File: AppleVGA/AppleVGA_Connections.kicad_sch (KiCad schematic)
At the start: 7 parts, among them J1 AppleIIBus, J2 VGA, J3 VGA, SW1 SW_Push

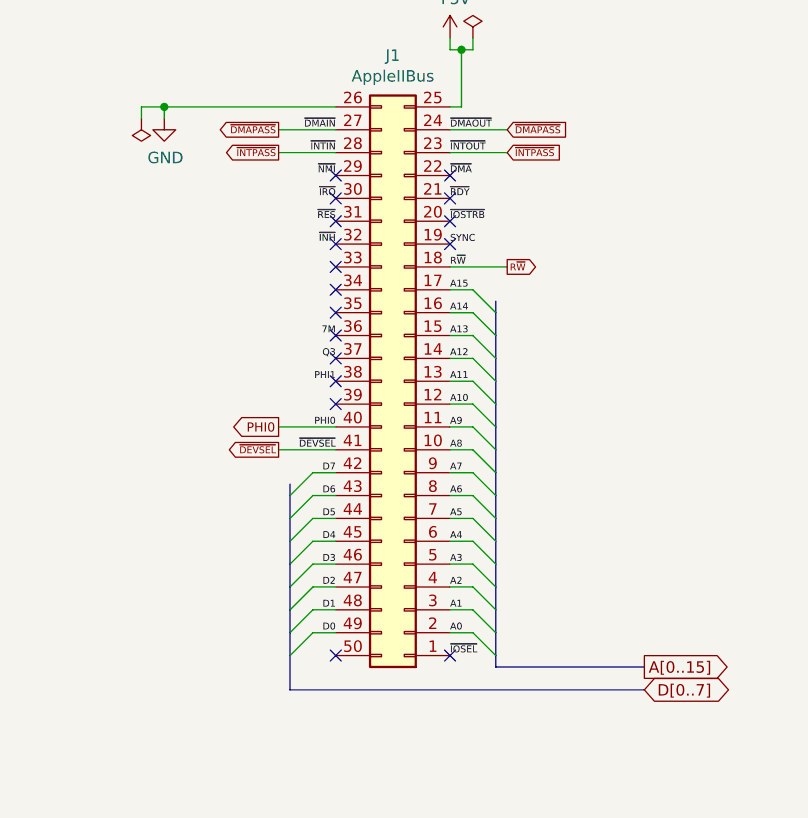
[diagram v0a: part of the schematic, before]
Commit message: Minor cleanups after KiCad6 conversion
* Fixed the 3.3v net symbol that changed in KiCad6
* Updated the Pico symbol & footprint to the latest version
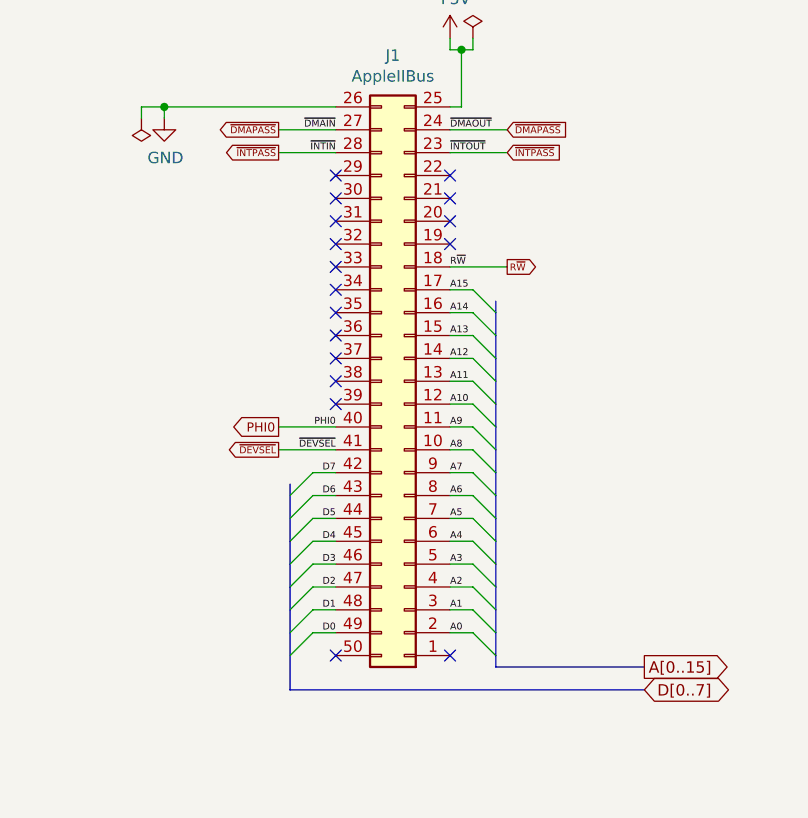
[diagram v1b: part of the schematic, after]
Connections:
- net +3V3 renamed +3.3V
- net 7M: no longer names the net of J1.36 (Pin_36)
- net PHI1: no longer names the net of J1.38 (Pin_38)
- net Q3: no longer names the net of J1.37 (Pin_37)
- net SYNC: no longer names the net of J1.19 (Pin_19)
- net ~{DMA}: no longer names the net of J1.22 (Pin_22)
- net ~{INH}: no longer names the net of J1.32 (Pin_32)
- net ~{IOSEL}: no longer names the net of J1.1 (Pin_1)
- net ~{IOSTRB}: no longer names the net of J1.20 (Pin_20)
- net ~{IRQ}: no longer names the net of J1.30 (Pin_30)
- net ~{NMI}: no longer names the net of J1.29 (Pin_29)
- net ~{RDY}: no longer names the net of J1.21 (Pin_21)
- net ~{RES}: no longer names the net of J1.31 (Pin_31)
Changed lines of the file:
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@@
   )
   (no_connect (at 60.96 77.47))
+  (no_connect (at 60.96 95.25))
+  (no_connect (at 60.96 90.17))
+  (no_connect (at 60.96 87.63))
+  (no_connect (at 73.66 77.47))
+  (no_connect (at 73.66 80.01))
+  (no_connect (at 73.66 74.93))
+  (no_connect (at 73.66 72.39))
   (no_connect (at 60.96 74.93))
-  (no_connect (at 60.96 87.63))
-  (no_connect (at 73.66 80.01))
+  (no_connect (at 60.96 72.39))
   (no_connect (at 60.96 125.73))
-  (no_connect (at 60.96 95.25))
-  (no_connect (at 73.66 77.47))
   (no_connect (at 207.01 86.36))
   (no_connect (at 191.77 93.98))
-  (no_connect (at 60.96 90.17))
-  (no_connect (at 73.66 125.73))
-  (no_connect (at 73.66 72.39))
+  (no_connect (at 60.96 80.01))
   (no_connect (at 60.96 82.55))
   (no_connect (at 207.01 81.28))
   (no_connect (at 60.96 97.79))
   (no_connect (at 191.77 96.52))
+  (no_connect (at 207.01 101.6))
   (no_connect (at 60.96 92.71))
-  (no_connect (at 207.01 101.6))
-  (no_connect (at 60.96 72.39))
-  (no_connect (at 60.96 80.01))
   (no_connect (at 60.96 85.09))
-  (no_connect (at 73.66 74.93))
+  (no_connect (at 73.66 125.73))
   (bus_entry (at 76.2 113.03) (size 2.54 2.54)
     (stroke (width 0) (type default) (color 0 0 0 0))
@@
     (effects (font (size 0.762 0.762)) (justify right bottom))
   )
-  (label "~{RES}" (at 60.96 77.47 180)
-    (effects (font (size 0.762 0.762)) (justify right bottom))
-  )
   (label "PHI0" (at 60.96 100.33 180)
     (effects (font (size 0.762 0.762)) (justify right bottom))
@@
     (effects (font (size 0.762 0.762)) (justify right bottom))
   )
-  (label "~{RDY}" (at 73.66 74.93 0)
-    (effects (font (size 0.762 0.762)) (justify left bottom))
-  )
-  (label "SYNC" (at 73.66 80.01 0)
-    (effects (font (size 0.762 0.762)) (justify left bottom))
-  )
   (label "A0" (at 73.66 123.19 0)
     (effects (font (size 0.762 0.762)) (justify left bottom))
@@
     (effects (font (size 0.762 0.762)) (justify left bottom))
   )
-  (label "~{IOSEL}" (at 73.66 125.73 0)
-    (effects (font (size 0.762 0.762)) (justify left bottom))
-  )
   (label "A11" (at 73.66 95.25 0)
     (effects (font (size 0.762 0.762)) (justify left bottom))
   )
-  (label "~{IRQ}" (at 60.96 74.93 180)
-    (effects (font (size 0.762 0.762)) (justify right bottom))
-  )
-  (label "PHI1" (at 60.96 95.25 180)
-    (effects (font (size 0.762 0.762)) (justify right bottom))
-  )
   (label "A5" (at 73.66 110.49 0)
     (effects (font (size 0.762 0.762)) (justify left bottom))
@@
     (effects (font (size 0.762 0.762)) (justify left bottom))
   )
-  (label "Q3" (at 60.96 92.71 180)
-    (effects (font (size 0.762 0.762)) (justify right bottom))
-  )
   (label "A13" (at 73.66 90.17 0)
     (effects (font (size 0.762 0.762)) (justify left bottom))
@@
     (effects (font (size 0.762 0.762)) (justify right bottom))
   )
-  (label "~{DMA}" (at 73.66 72.39 0)
-    (effects (font (size 0.762 0.762)) (justify left bottom))
-  )
   (label "A1" (at 73.66 120.65 0)
     (effects (font (size 0.762 0.762)) (justify left bottom))
@@
     (effects (font (size 0.762 0.762)) (justify right bottom))
   )
-  (label "~{NMI}" (at 60.96 72.39 180)
-    (effects (font (size 0.762 0.762)) (justify right bottom))
-  )
   (label "~{INTIN}" (at 60.96 69.85 180)
     (effects (font (size 0.762 0.762)) (justify right bottom))
@@
     (effects (font (size 0.762 0.762)) (justify left bottom))
   )
-  (label "~{INH}" (at 60.96 80.01 180)
-    (effects (font (size 0.762 0.762)) (justify right bottom))
-  )
   (label "~{INTOUT}" (at 73.66 69.85 0)
     (effects (font (size 0.762 0.762)) (justify left bottom))
   )
-  (label "7M" (at 60.96 90.17 180)
-    (effects (font (size 0.762 0.762)) (justify right bottom))
-  )
   (label "A8" (at 73.66 102.87 0)
     (effects (font (size 0.762 0.762)) (justify left bottom))
@@
   (label "~{DEVSEL}" (at 60.96 102.87 180)
     (effects (font (size 0.762 0.762)) (justify right bottom))
-  )
-  (label "~{IOSTRB}" (at 73.66 77.47 0)
-    (effects (font (size 0.762 0.762)) (justify left bottom))
   )
   (label "A6" (at 73.66 107.95 0)
@@
     (pin "2")
   )
-  (symbol (lib_id "AppleVGA-rescue:+3.3V-power") (at 39.37 166.37 0) (unit 1)
+  (symbol (lib_id "power:+3.3V") (at 39.37 166.37 0) (unit 1)
     (in_bom yes) (on_board yes)
     (property "Reference" "#PWR0115" (id 0) (at 39.37 170.18 0)
